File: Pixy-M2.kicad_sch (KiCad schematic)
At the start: 56 parts, among them J1 USB_C_Receptacle_USB2.0_14P, J2 Conn_01x22_Pin, J3 Conn_01x22_Pin, J4 SM06B-SRSS-TB, J5 SM06B-SRSS-TB, J6 SM06B-SRSS-TB, J7 SM06B-SRSS-TB, Q1 AO4407A, SW1 SW_Push, SW2 SW_Push, SW3 JS102011SAQN, U1 ESP32-S3-WROOM-1-N16, U2 USBLC6-2SC6, U3 AP63203WU

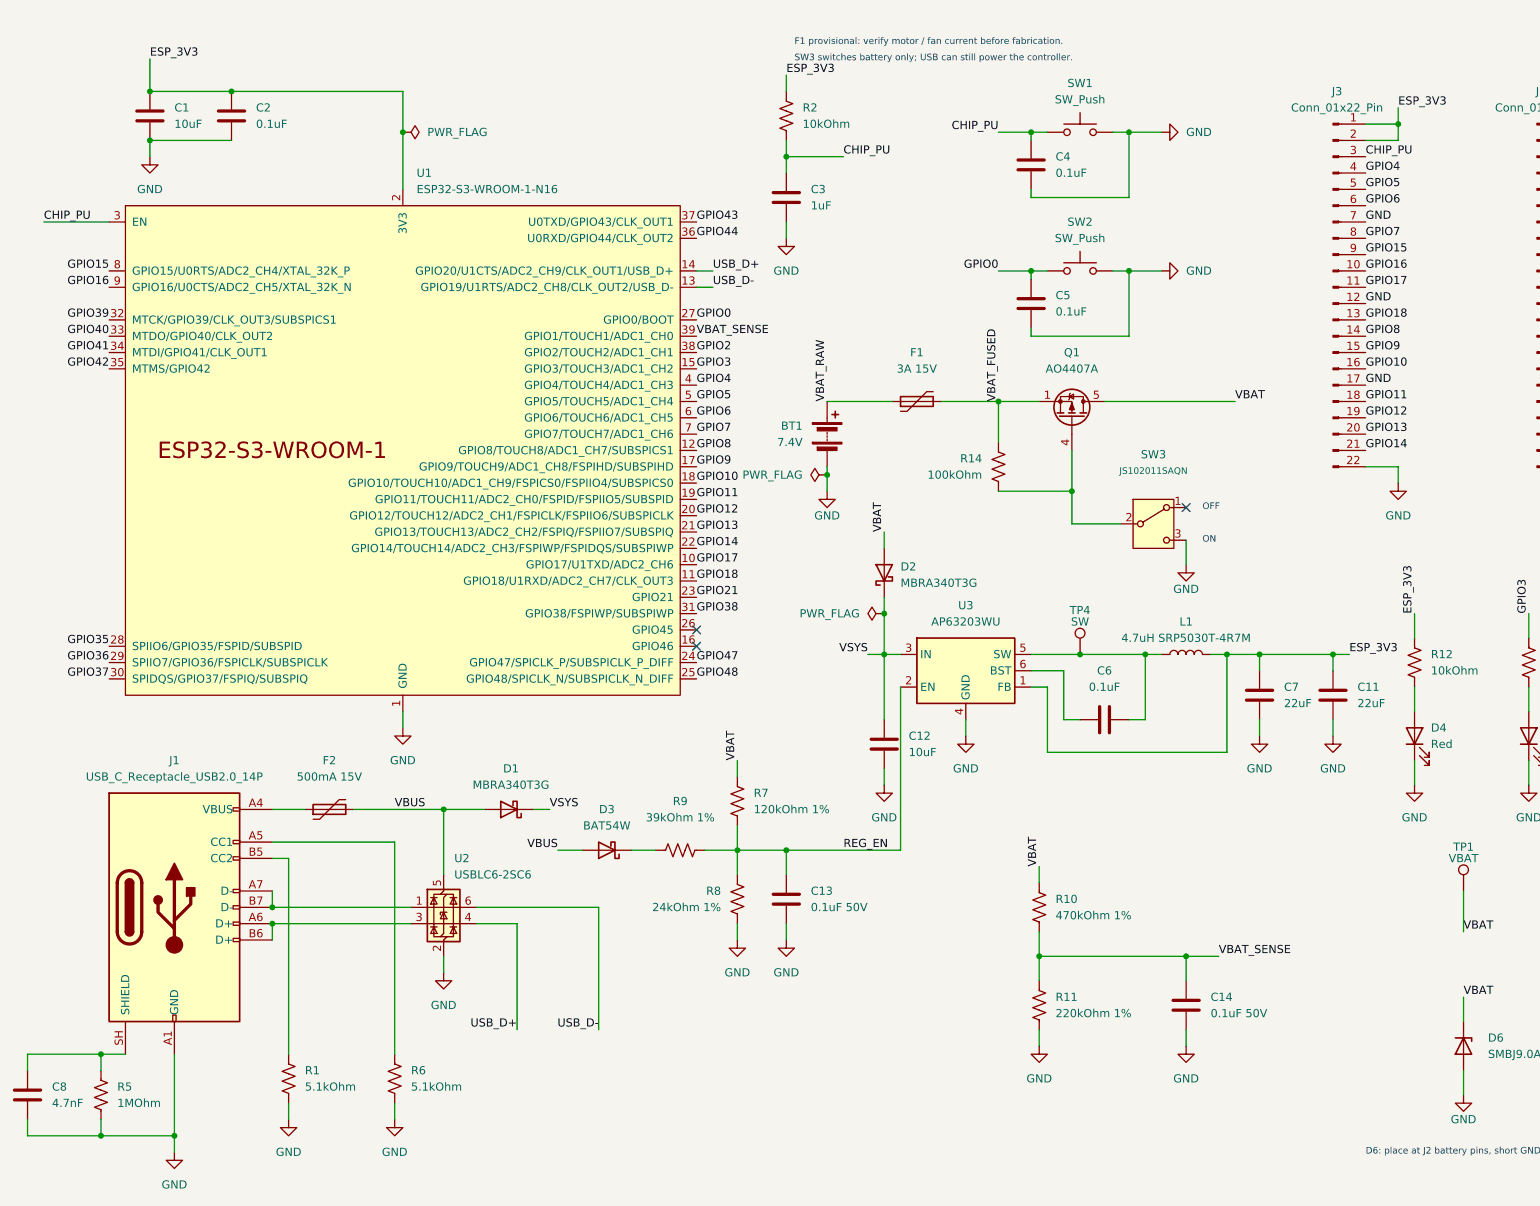
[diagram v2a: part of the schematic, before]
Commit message: Specify capacitor voltage ratings and fix the VSYS input network (issue 8)
Every capacitor now states its rating in the Value field, following C13's
precedent so it is visible on the sheet. Ten caps gained one; C13/C14/C15/C16
already had theirs.

Two changes go beyond adding text, and both move Value and Footprint
together rather than leaving a half-updated component:

C12: 10uF 0805 -> 22uF 25V 1206. Checked against the AP63203 datasheet
(DS41326 Rev 3-2) rather than this issue's own note, which was wrong: it
claimed the part wants ~2x10uF effective input capacitance. Table 2 specifies
C1 (input) = 10uF, and the Input Capacitor section says ">10uF is sufficient
for most applications". The 2x22uF in that table is the OUTPUT, which C7||C11
already match. Meeting 10uF effective at 8.4V bias is the real constraint: a
25V 10uF 0805 derates to ~3-4uF, so two would still fall short at ~7-9uF,
while a 25V 22uF 1206 retains ~11-13uF. One part meets it where two did not,
with one fewer placement inside the tight input loop.

C8: 4.7nF 0603 -> 4.7nF 1kV 1206. This issue said "everything else: minimum
16V", which is wrong for C8 -- it is the USB shield cap and an ESD path, not
a bias node. An IEC 61000-4-2 8kV contact discharge dumps a 150pF source into
it, so the node divides as 8kV x 150pF/(150pF + 4.7nF) ~= 250V across C8. A
16V or 50V part is destroyed. 1kV is not available at 4.7nF in 0603, so the
footprint moved with the rating.

Adds C17 (0.1uF 25V, 0603) as the high-frequency bypass the datasheet's pin-3
description and layout section call for -- "place the VIN capacitors as close
to the device as possible", plural.

Also records the datasheet's 2oz-copper and via-stitching requests in the
board stackup section.

Verified:
- Netlist diff vs previous commit: exactly two changes, C17.1 -> /VSYS and
  C17.2 -> GND. Net count steady at 62, no new auto-named nets, every other
  net identical.
- ERC unchanged at 0 errors, 0 warnings.
- Sheet rendered and inspected three tim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
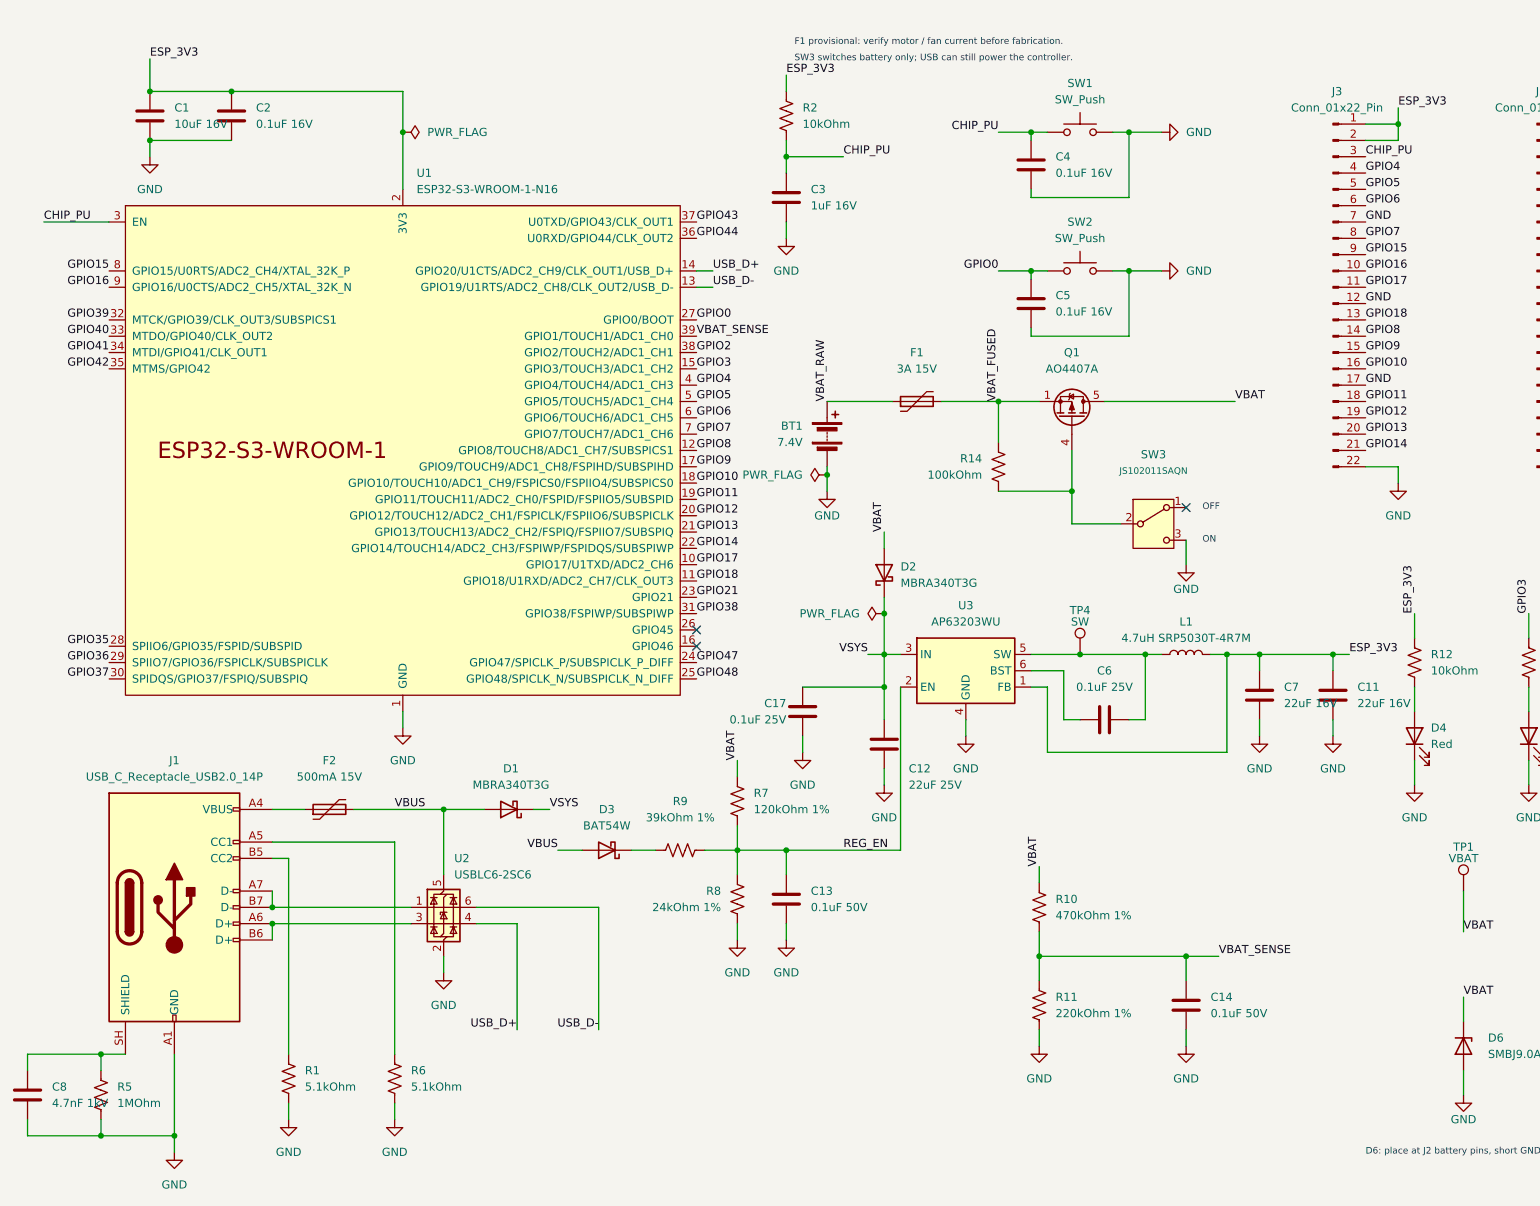
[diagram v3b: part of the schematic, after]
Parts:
- added C17: 0.1uF 25V, Capacitor_SMD:C_0603_1608Metric, symbol Device:C
- C1: value 10uF -> 10uF 16V
- C11, C7: value 22uF -> 22uF 16V
- C12: value 10uF -> 22uF 25V; footprint Capacitor_SMD:C_0805_2012Metric -> Capacitor_SMD:C_1206_3216Metric
- C2, C4, C5: value 0.1uF -> 0.1uF 16V
- C3: value 1uF -> 1uF 16V
- C6: value 0.1uF -> 0.1uF 25V
- C8: value 4.7nF -> 4.7nF 1kV; footprint Capacitor_SMD:C_0603_1608Metric -> Capacitor_SMD:C_1206_3216Metric
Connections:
- net GND: now also C17.2
- net VSYS: now also C17.1
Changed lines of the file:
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@@
 	(wire
 		(pts
+			(xy 156.21 118.11) (xy 143.51 118.11)
+		)
+		(stroke
+			(width 0)
+			(type default)
+		)
+	)
+	(wire
+		(pts
+			(xy 143.51 125.73) (xy 143.51 128.27)
+		)
+		(stroke
+			(width 0)
+			(type default)
+		)
+	)
+	(junction
+		(at 156.21 118.11)
+		(diameter 0)
+		(color 0 0 0 0)
+	)
+	(wire
+		(pts
 			(xy 156.21 130.81) (xy 156.21 133.35)
 		)
@@
 		(fields_autoplaced yes)
 		(property "Reference" "C12"
-			(at 160.02 125.7299 0)
+			(at 160.02 130.81 0)
 			(show_name no)
 			(do_not_autoplace no)
@@
 			)
 		)
-		(property "Value" "10uF"
-			(at 160.02 128.2699 0)
+		(property "Value" "22uF 25V"
+			(at 160.02 133.35 0)
 			(show_name no)
 			(do_not_autoplace no)
@@
 			)
 		)
-		(property "Footprint" "Capacitor_SMD:C_0805_2012Metric"
+		(property "Footprint" "Capacitor_SMD:C_1206_3216Metric"
 			(at 157.1752 130.81 0)
 			(hide yes)
@@
 			)
 		)
-		(property "Value" "22uF"
+		(property "Value" "22uF 16V"
 			(at 229.87 120.6499 0)
 			(show_name no)
@@
 			)
 		)
-		(property "Value" "0.1uF"
+		(property "Value" "0.1uF 16V"
 			(at 58.42 30.4799 0)
 			(show_name no)
@@
 			)
 		)
-		(property "Value" "0.1uF"
+		(property "Value" "0.1uF 25V"
 			(at 190.5 118.11 90)
 			(show_name no)
@@
 			)
 		)
-		(property "Value" "0.1uF"
+		(property "Value" "0.1uF 16V"
 			(at 182.88 38.0999 0)
 			(show_name no)
@@
 			)
 		)
-		(property "Value" "0.1uF"
+		(property "Value" "0.1uF 16V"
 			(at 182.88 59.6899 0)
 			(show_name no)
@@
 			)
 		)
-		(property "Value" "10uF"
+		(property "Value" "10uF 16V"
 			(at 45.72 30.4799 0)
 			(show_name no)
@@
 			)
 		)
-		(property "Value" "22uF"
+		(property "Value" "22uF 16V"
 			(at 218.44 120.6499 0)
 			(show_name no)
@@
 			)
 		)
-		(property "Value" "1uF"
+		(property "Value" "1uF 16V"
 			(at 144.78 43.1799 0)
 			(show_name no)
@@
 	)
 	(symbol
+		(lib_id "Device:C")
+		(at 143.51 121.92 0)
+		(unit 1)
+		(body_style 1)
+		(exclude_from_sim no)
+		(in_bom yes)
+		(on_board yes)
+		(in_pos_files yes)
+		(dnp no)
+		(property "Reference" "C17"
+			(at 140.97 120.65 0)
+			(show_name no)
+			(do_not_autoplace no)
+			(effects
+				(font
+					(size 1.27 1.27)
+				)
+				(justify right)
+			)
+		)
+		(property "Value" "0.1uF 25V"
+			(at 140.97 123.19 0)
+			(show_name no)
+			(do_not_autoplace no)
+			(effects
+				(font
+					(size 1.27 1.27)
+				)
+				(justify right)
+			)
+		)
+		(property "Footprint" "Capacitor_SMD:C_0603_1608Metric"
+			(at 143.51 121.92 0)
+			(hide yes)
+			(show_name no)
+			(do_not_autoplace no)
+			(effects
+				(font
+					(size 1.27 1.27)
+				)
+			)
+		)
+		(property "Datasheet" ""
+			(at 143.51 121.92 0)
+			(hide yes)
+			(show_name no)
+			(do_not_autoplace no)
+			(effects
+				(font
+					(size 1.27 1.27)
+				)
+			)
+		)
+		(property "Description" "VSYS high-frequency bypass. Place hard against U3.3 (IN)."
+			(at 143.51 121.92 0)
+			(hide yes)
+			(show_name no)
+			(do_not_autoplace no)
+			(effects
+				(font
+					(size 1.27 1.27)
+				)
+			)
+		)
+		(pin "1"
+		)
+		(pin "2"
+		)
+		(instances
+			(project "Pixy-M2"
+				(path "/fefb2c5c-cd05-4562-bf27-32a51f81fd04"
+					(reference "C17")
+					(unit 1)
+				)
+			)
+		)
+	)
+	(symbol
+		(lib_id "power:GND")
+		(at 143.51 128.27 0)
+		(unit 1)
+		(body_style 1)
+		(exclude_from_sim no)
+		(in_bom yes)
+		(on_board yes)
+		(in_pos_files yes)
+		(dnp no)
+		(fields_autoplaced yes)
+		(property "Reference" "#PWR033"
+			(at 143.51 134.62 0)
+			(hide yes)
+			(show_name no)
+			(do_not_autoplace no)
+			(effects
+				(font
+					(size 1.27 1.27)
+				)
+			)
+		)
+		(property "Value" "GND"
+			(at 143.51 133.35 0)
+			(show_name no)
+			(do_not_autoplace no)
+			(effects
+				(font
+					(size 1.27 1.27)
+				)
+			)
+		)
+		(property "Footprint" ""
+			(at 143.51 128.27 0)
+			(hide yes)
+			(show_name no)
+			(do_not_autoplace no)
+			(effects
+				(font
+					(size 1.27 1.27)
+				)
+			)
+		)
+		(property "Datasheet" ""
+			(at 143.51 128.27 0)
+			(hide yes)
+			(show_name no)
+			(do_not_autoplace no)
+			(effects
+				(font
+					(size 1.27 1.27)
+				)
+			)
+		)
+		(property "Description" "Power symbol creates a global label with name \"GND\" , ground"
+			(at 143.51 128.27 0)
+			(hide yes)
+			(show_name no)
+			(do_not_autoplace no)
+			(effects
+				(font
+					(size 1.27 1.27)
+				)
+			)
+		)
+		(pin "1"
+		)
+		(instances
+			(project "Pixy-M2"
+				(path "/fefb2c5c-cd05-4562-bf27-32a51f81fd04"
+					(reference "#PWR033")
+					(unit 1)
+				)
+			)
+		)
+	)
+	(symbol
 		(lib_id "power:GND")
 		(at 156.21 133.35 0)
@@
 			)
 		)
-		(property "Value" "4.7nF"
+		(property "Value" "4.7nF 1kV"
 			(at 26.67 182.8799 0)
 			(show_name no)
@@
 			)
 		)
-		(property "Footprint" "Capacitor_SMD:C_0603_1608Metric"
+		(property "Footprint" "Capacitor_SMD:C_1206_3216Metric"
 			(at 23.8252 185.42 0)
 			(hide yes)

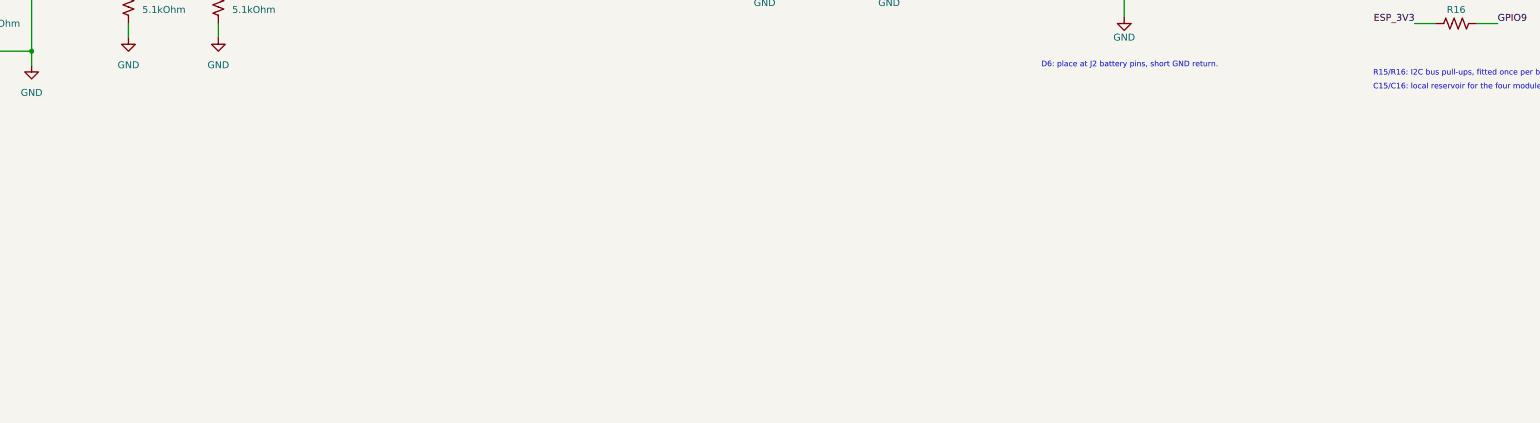
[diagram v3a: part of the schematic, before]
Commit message: Add on-board N20 motor drive: DRV8231A x2, encoders, connectors (issues 15, 16)
Implements the motor half of issue 15 and closes issue 16. 14 parts added:
U4/U5 drivers, C18/C20 VM bypass, C19/C21 bulk, R17/R18 current-sense,
R19-R22 encoder pull-ups, J8/J9 motor+encoder connectors.

Driver: TI DRV8231A (DRV8231ADSG, WSON-8 2x2mm). The brief was headroom
above D6's 15.4V clamp, and that eliminated the obvious candidates: DRV8833
has an 11.8V absolute maximum and TB6612FNG 15V, both below the clamp.
DRV8874/DRV8876 (40V, 200mOhm) are better on RDS(on) but have no stock KiCad
symbol. Verified against the TI datasheet: VM 4.5-33V operating with a 35V
absolute maximum (2.3x the clamp), 3.7A peak, 300mOhm HS + 300mOhm LS,
integrated current sense and regulation, WSON-8, RthJA 66.5 C/W.

The 4.5V minimum matters: the board's own UVLO runs down to 5.94V, so
DRV8871, DRV8848 and A4950 (6.5V/8V/7.5V minimums) would be out of spec
across part of the usable pack range.

IN1/IN2 have internal 100k pulldowns, so both motors stay off while the
ESP32-S3's GPIOs float at reset.

Current limit: VREF tied to ESP_3V3 and R17/R18 = 1.5k give
ITRIP = 3.3/(1500u x 1500) = 1.47A, with IPROPI reading 2.25 V/A into GPIO2
(ADC1_CH1) and GPIO10 (ADC1_CH9) -- ADC1 because ADC2 is unusable with Wi-Fi.
1.47A is set to protect the driver, not the motor: an unregulated stall draws
8.4/(3.75+0.6) = 1.93A, which is 2.24W into a 66.5 C/W package and thermal
shutdown, against 1.29W when regulated. Torque is proportional to current, so
the limit still gives ~92% of rated stall torque, and it keeps the JST-PH
contacts (2A each) inside their rating, which the 1.93A stall would not.

This is the hardware half of the stall protection issue 17 asks firmware for.

Connectors mirror the encoder module pin order (1=M1 2=GND 3=OUTA 4=OUTB
5=VCC 6=M2) so the loom is straight-through, the same principle as J4-J7.

Corrects a KiCad library bug locally: Driver_Motor:DRV8231ADSG types pin 8
(OUT2) as power_in while 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
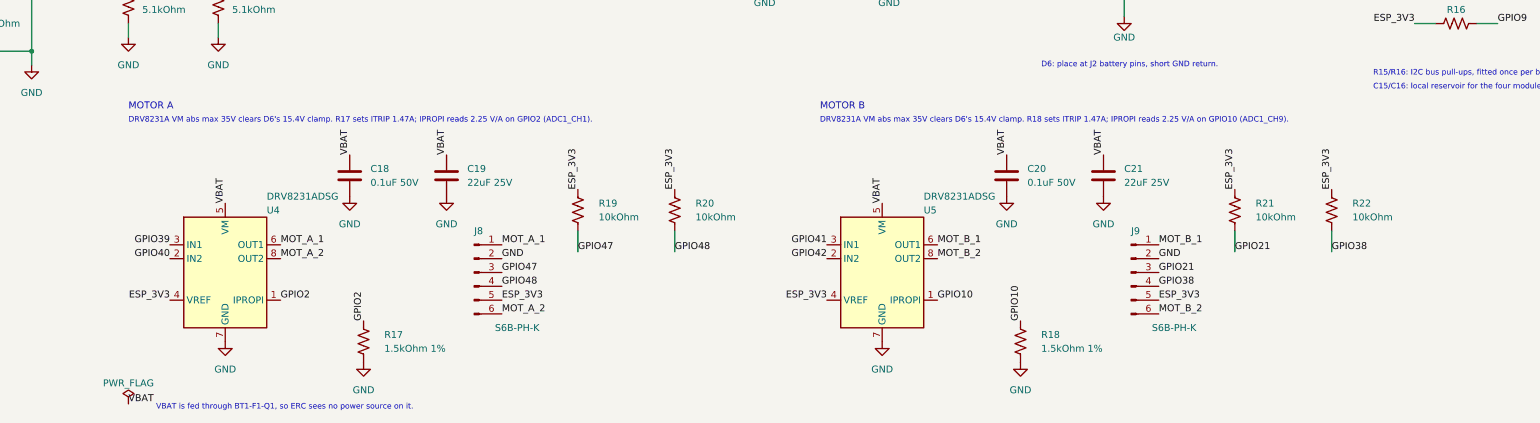
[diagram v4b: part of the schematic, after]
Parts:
- added C18, C20: 0.1uF 50V, Capacitor_SMD:C_0603_1608Metric, symbol Device:C
- added C19, C21: 22uF 25V, Capacitor_SMD:C_1206_3216Metric, symbol Device:C
- added J8, J9: S6B-PH-K, Connector_JST:JST_PH_S6B-PH-K_1x06_P2.00mm_Horizontal, symbol Connector:Conn_01x06_Pin
- added R17, R18: 1.5kOhm 1%, Resistor_SMD:R_0805_2012Metric, symbol Device:R_US
- added R19, R20, R21, R22: 10kOhm, Resistor_SMD:R_0805_2012Metric, symbol Device:R_US
- added U4, U5: DRV8231ADSG, Package_SON:Texas_DSG0008A_WSON-8-1EP_2x2mm_P0.5mm_EP0.9x1.6mm, symbol Driver_Motor:DRV8231ADSG
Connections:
- net ESP_3V3: now also J8.5 (Pin_5), J9.5 (Pin_5), R19.1, R20.1, R21.1, R22.1, U4.4 (VREF), U5.4 (VREF)
- net GND: now also C18.2, C19.2, C20.2, C21.2, J8.2 (Pin_2), J9.2 (Pin_2), R17.2, R18.2, U4.7 (GND), U4.9 (GND), U5.7 (GND), U5.9 (GND)
- net GPIO10: now also R18.1, U5.1 (IPROPI)
- net GPIO2: now also R17.1, U4.1 (IPROPI)
- net GPIO21: now also J9.3 (Pin_3), R21.2
- net GPIO38: now also J9.4 (Pin_4), R22.2
- net GPIO39: now also U4.3 (IN1)
- net GPIO40: now also U4.2 (IN2)
- net GPIO41: now also U5.3 (IN1)
- net GPIO42: now also U5.2 (IN2)
- net GPIO47: now also J8.3 (Pin_3), R19.2
- net GPIO48: now also J8.4 (Pin_4), R20.2
- net VBAT: now also C18.1, C19.1, C20.1, C21.1, U4.5 (VM), U5.5 (VM)
- new net MOT_A_1: J8.1 (Pin_1), U4.6 (OUT1)
- new net MOT_A_2: J8.6 (Pin_6), U4.8 (OUT2)
- new net MOT_B_1: J9.1 (Pin_1), U5.6 (OUT1)
- new net MOT_B_2: J9.6 (Pin_6), U5.8 (OUT2)
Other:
- note added: "DRV8231A VM abs max 35V clears D6's 15.4V clamp. R17 sets ITRIP 1.47A; IPROPI reads 2.25 V/A on GPIO2 (ADC1_CH1)."
- note added: "DRV8231A VM abs max 35V clears D6's 15.4V clamp. R18 sets ITRIP 1.47A; IPROPI reads 2.25 V/A on GPIO10 (ADC1_CH9)."
- note added: "MOTOR A"
- note added: "MOTOR B"
- note added: "VBAT is fed through BT1-F1-Q1, so ERC sees no power source on it."
